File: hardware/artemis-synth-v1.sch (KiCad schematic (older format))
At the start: 55 parts, among them IC1 ATMEGA328P, J1 USB_2, J2 AVR-ISP-6, SW10 SWITCH_PUSH_CW, SW11 SWITCH_PUSH_CW, SW2 SWITCH_PUSH_CW, SW3 SWITCH_PUSH_CW, SW4 SWITCH_PUSH_CW, SW5 SWITCH_PUSH_CW, SW6 SWITCH_PUSH_CW, SW7 SWITCH_PUSH_CW, SW8 SWITCH_PUSH_CW, SW9 SWITCH_PUSH_CW, U1 MCP4921, U2 TDA2722M, X1 16MHz

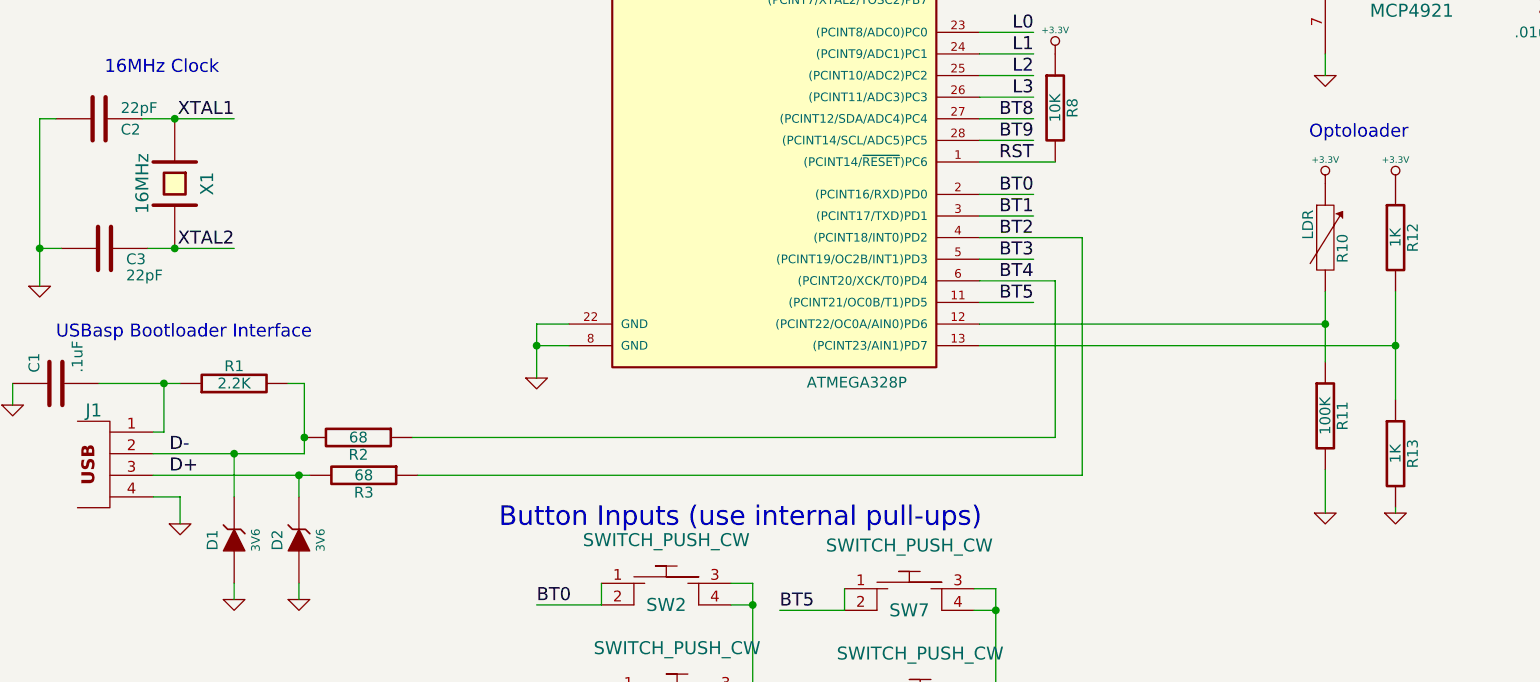
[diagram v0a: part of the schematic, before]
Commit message: added sequencer
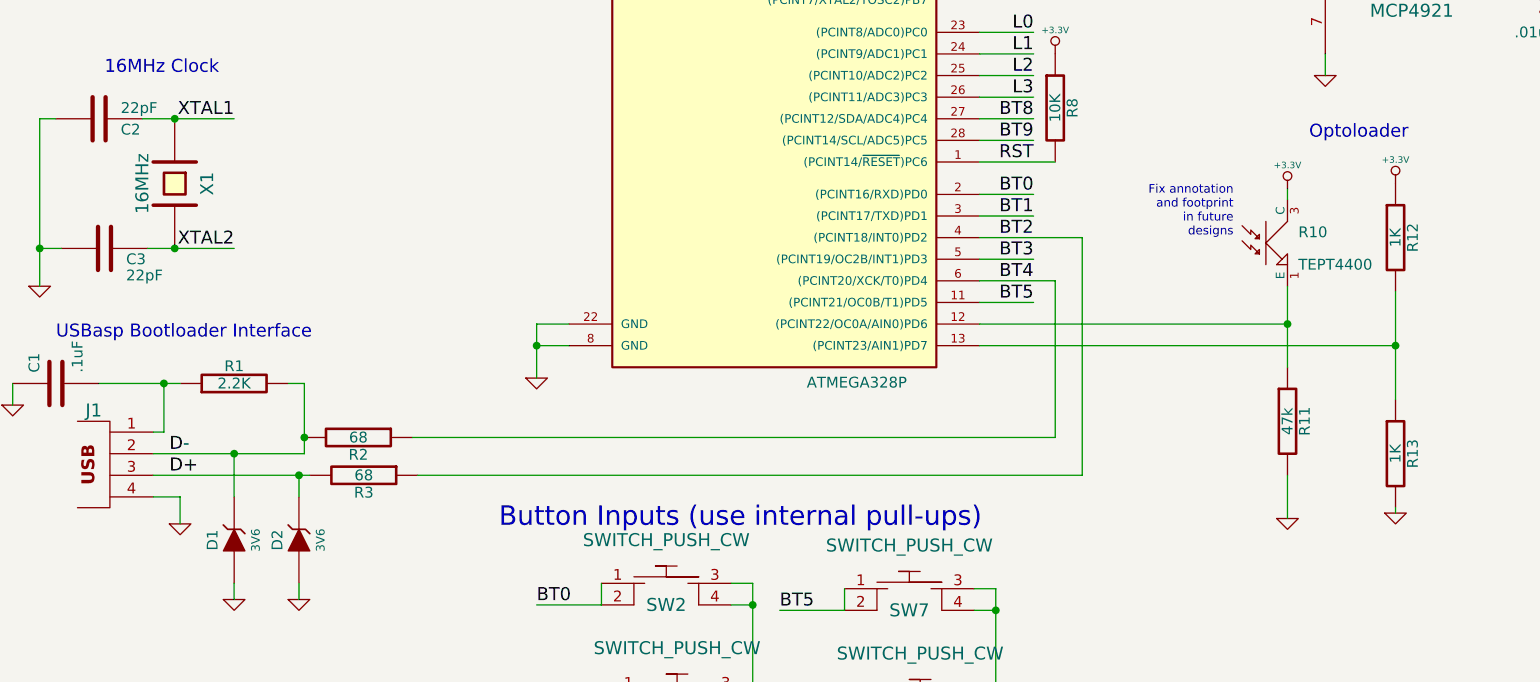
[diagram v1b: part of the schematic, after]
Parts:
- removed R10: LDR, SIL-2, symbol RVAR
- added R10: TEPT4400, symbol OPTO_NPN
- R11: value 100K -> 47k
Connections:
- net +3.3V: now also R10.3 (C)
- net at IC1.12 ((PCINT22/OC0A/AIN0)PD6), R11.1: now also R10.1 (E)
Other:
- note added: "Fix annotation\nand footprint\nin future\ndesigns\n"
- moved on the sheet: R11

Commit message: Firmware, updated some other things...
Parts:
- U2: value TDA2722M -> TDA2822M
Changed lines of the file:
@@
-EESchema Schematic File Version 2  date Wed 18 Jul 2012 10:01:27 AM EDT
+EESchema Schematic File Version 2  date Thu 19 Jul 2012 05:37:40 PM EDT
 LIBS:power
 LIBS:device
@@
 Sheet 1 1
 Title ""
-Date "18 jul 2012"
+Date "19 jul 2012"
 Rev ""
 Comp ""
@@
 P 9075 2575
 F 0 "U2" H 9625 2375 60  0000 C CNN
-F 1 "TDA2722M" H 9800 2475 60  0000 C CNN
+F 1 "TDA2822M" H 9800 2475 60  0000 C CNN
 F 2 "DIP-8__300" H 9800 2575 60  0001 C CNN
 	1    9075 2575
